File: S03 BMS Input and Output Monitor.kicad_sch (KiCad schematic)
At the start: 29 parts, among them Q4 DMP3018SFV, Q5 DMP3018SFV, U1 LTC1960

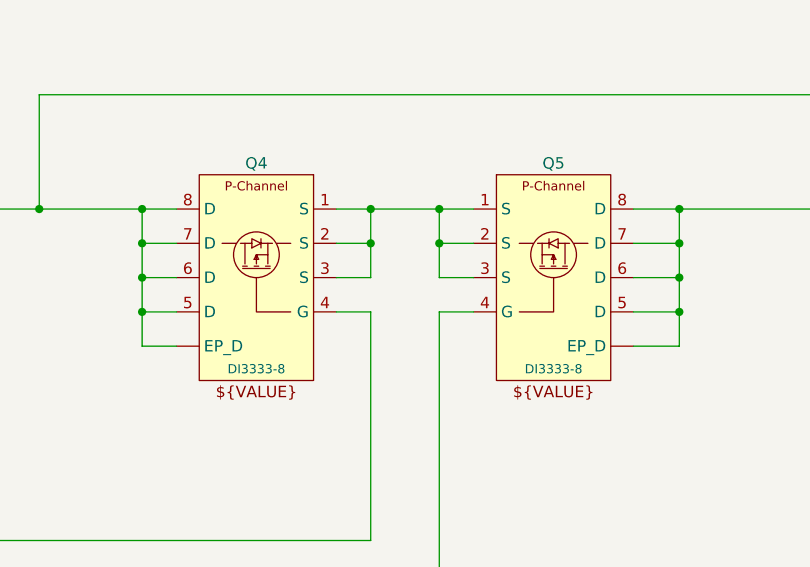
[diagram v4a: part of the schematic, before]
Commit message: Fit DMP3007SCG battery FETs and 1210 snubber resistors
- Q4, Q5, Q12-Q15: DMP3018SFV -> DMP3007SCG-13 (V-DFN3333-8 Type B) on
  KiCad's standard Package_SON:Diodes_PowerDI3333-8, which matches Diodes'
  Type B suggested land apart from 0.1 mm more toe per pad row. The new
  project symbol keeps the old pin positions and numbers D pins 5-8 and
  EP_D all 5, the footprint's single drain pad; all were already one net.
  The unused DMP3018SFV symbol is removed from the project library.
- R41, R45 (SW1/SW2 snubbers): 2.2R 1206 1/4 W -> 2.2R 1% 1210 1/2 W, any
  standard thick film. R41 runs at 75% (0.38 W worst case), R45 at 33%.
- README design-change rows for both.

The PCB still needs Update PCB from Schematic for these and the DAQ UVLO
parts.

Co-Authored-By: Claude Opus 5.5 <noreply@anthropic.com>
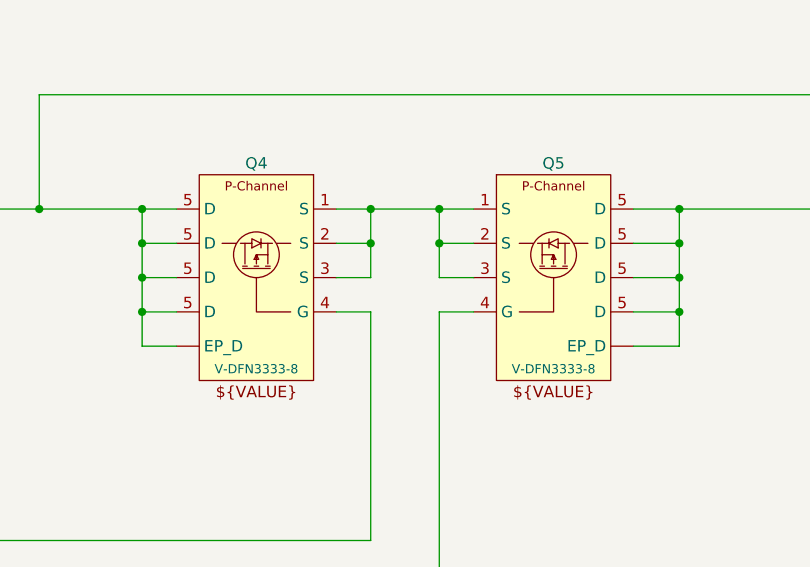
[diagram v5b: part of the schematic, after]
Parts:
- Q4, Q5: value DMP3018SFV -> DMP3007SCG-13; footprint EVO2513-0_5_0-import-fps:Power DI3333-8 B3.3 x 3.3 P0.65 Tab 8-Pin -> Package_SON:Diodes_PowerDI3333-8; symbol Lattech Systems:Transistor P-Channel MOSFET 30V DMP3018SFV Power DI3333-8 -> Lattech Systems:Transistor P-Channel MOSFET 30V DMP3007SCG V-DFN3333-8; ALTIUM_FOOTPRINT DI3333-8 -> V-DFN3333-8; ALTIUM_VALUE DMP3018SFV -> DMP3007SCG-13; MANUFACTURER_PN DMP3018SFV -> DMP3007SCG-13
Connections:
- net DCPATH: no longer Q5.6 (D), Q5.7 (D), Q5.8 (D), Q5.9 (EP_D)
- net DCSENSED: no longer Q4.6 (D), Q4.7 (D), Q4.8 (D), Q4.9 (EP_D)
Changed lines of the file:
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@@
 	)
 	(symbol
-		(lib_id "Lattech Systems:Transistor P-Channel MOSFET  30V DMP3018SFV Power DI3333-8")
+		(lib_id "Lattech Systems:Transistor P-Channel MOSFET 30V DMP3007SCG V-DFN3333-8")
 		(at 260.35 83.82 0)
 		(mirror y)
@@
 			)
 		)
-		(property "Value" "DMP3018SFV"
+		(property "Value" "DMP3007SCG-13"
 			(at 247.65 82.55 0)
 			(hide yes)
@@
 			)
 		)
-		(property "Footprint" "EVO2513-0_5_0-import-fps:Power DI3333-8 B3.3 x 3.3 P0.65 Tab 8-Pin"
+		(property "Footprint" "Package_SON:Diodes_PowerDI3333-8"
 			(at 260.35 83.82 0)
 			(hide yes)
@@
 			)
 		)
-		(property "Description" "Transistor P-Channel MOSFET  30V DMP3018SFV Power DI3333-8"
+		(property "Description" "Transistor P-Channel MOSFET 30V DMP3007SCG-13 V-DFN3333-8 (Type B)"
 			(at 260.35 83.82 0)
 			(hide yes)
@@
 			)
 		)
-		(property "ALTIUM_FOOTPRINT" "DI3333-8"
+		(property "ALTIUM_FOOTPRINT" "V-DFN3333-8"
 			(at 251.46 101.5998 0)
 			(show_name no)
@@
 			)
 		)
-		(property "ALTIUM_VALUE" "DMP3018SFV"
+		(property "ALTIUM_VALUE" "DMP3007SCG-13"
 			(at 270.002 81.026 0)
 			(hide yes)
@@
 			)
 		)
-		(property "MANUFACTURER_PN" "DMP3018SFV"
+		(property "MANUFACTURER_PN" "DMP3007SCG-13"
 			(at 259.842 77.47 0)
 			(hide yes)
@@
 		(pin "5"
 		)
-		(pin "7"
-		)
 		(pin "4"
 		)
 		(pin "2"
-		)
-		(pin "6"
-		)
-		(pin "8"
-		)
-		(pin "9"
 		)
 		(instances
@@
 	)
 	(symbol
-		(lib_id "Lattech Systems:Transistor P-Channel MOSFET  30V DMP3018SFV Power DI3333-8")
+		(lib_id "Lattech Systems:Transistor P-Channel MOSFET 30V DMP3007SCG V-DFN3333-8")
 		(at 275.59 83.82 0)
 		(unit 1)
@@
 			)
 		)
-		(property "Value" "DMP3018SFV"
+		(property "Value" "DMP3007SCG-13"
 			(at 288.29 82.55 0)
 			(hide yes)
@@
 			)
 		)
-		(property "Footprint" "EVO2513-0_5_0-import-fps:Power DI3333-8 B3.3 x 3.3 P0.65 Tab 8-Pin"
+		(property "Footprint" "Package_SON:Diodes_PowerDI3333-8"
 			(at 275.59 83.82 0)
 			(hide yes)
@@
 			)
 		)
-		(property "Description" "Transistor P-Channel MOSFET  30V DMP3018SFV Power DI3333-8"
+		(property "Description" "Transistor P-Channel MOSFET 30V DMP3007SCG-13 V-DFN3333-8 (Type B)"
 			(at 275.59 83.82 0)
 			(hide yes)
@@
 			)
 		)
-		(property "ALTIUM_FOOTPRINT" "DI3333-8"
+		(property "ALTIUM_FOOTPRINT" "V-DFN3333-8"
 			(at 284.48 101.5998 0)
 			(show_name no)
@@
 			)
 		)
-		(property "ALTIUM_VALUE" "DMP3018SFV"
+		(property "ALTIUM_VALUE" "DMP3007SCG-13"
 			(at 265.938 81.026 0)
 			(hide yes)
@@
 			)
 		)
-		(property "MANUFACTURER_PN" "DMP3018SFV"
+		(property "MANUFACTURER_PN" "DMP3007SCG-13"
 			(at 275.082 77.47 0)
 			(hide yes)
@@
 			)
 		)
-		(pin "6"
-		)
 		(pin "3"
 		)
@@
 		(pin "5"
 		)
-		(pin "7"
-		)
 		(pin "4"
 		)
 		(pin "2"
 		)
-		(pin "8"
-		)
-		(pin "9"
-		)
 		(instances

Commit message: R16 to 3 mOhm; note the DAQ/EXT current limits; keep Q18
- R16 0.005R -> 0.003R (Bourns CRE2512-FZ-R003E-3): the LTC1960 breaker
  moves from 18-23 A to 30-38 A. Peak 12 V load is about 7.5 A SBC (90 W)
  + 2.5 A J3 + DAQ, and QE29 packs at ~21 A would sit inside the old trip
  window. S03 note updated.
- S07 note: R53/R71 (1K, 6.6 A limit, up to 7.1 A) exceed J6/J5's 6.5 A
  single contact; raise them to 1.2K or more once the DAQ and EXT loads
  are known. Left at 1K for now: DAQ runs a stand-in, EXT is unused.
- README rows for R16, R53/R71 and Q18 (CSD17304Q3 kept: it works and 15
  units are in field test).

Co-Authored-By: Claude Opus 5.5 <noreply@anthropic.com>
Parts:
- R16: value 0.005R -> 0.003R; ALTIUM_VALUE 0.005R -> 0.003R; MANUFACTURER (none) -> Bourns; MANUFACTURER_PN CRE2512-FZ-R005E-3 -> CRE2512-FZ-R003E-3
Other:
- note added: "R16 breaker latches: 90-115 mV for 15 ms (30-38 A with 3 mR) opens every PowerPath switch, including DC, and sets FA. It clears only when all sources are removed and VPLUS falls below UVLO. ED29 test packs trip at 8 A each (measured); QE29 production packs at 10.5 A. Any figure keyed to 10.5 A applies to QE29 only."
- note removed: "R16 breaker latches: 90-115 mV for 15 ms opens every PowerPath switch, including DC, and sets FA. It clears only when all sources are removed and VPLUS falls below UVLO. ED29 test packs trip at 8 A each (measured); QE29 production packs at 10.5 A. Any figure keyed to 10.5 A applies to QE29 only."
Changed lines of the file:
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@@
 		)
 	)
-	(text "R16 breaker latches: 90-115 mV for 15 ms opens every PowerPath\nswitch, including DC, and sets FA. It clears only when all sources\nare removed and VPLUS falls below UVLO.\nED29 test packs trip at 8 A each (measured); QE29 production packs\nat 10.5 A. Any figure keyed to 10.5 A applies to QE29 only."
+	(text "R16 breaker latches: 90-115 mV for 15 ms (30-38 A with 3 mR)\nopens every PowerPath switch, including DC, and sets FA. It\nclears only when all sources are removed and VPLUS falls below UVLO.\nED29 test packs trip at 8 A each (measured); QE29 production packs\nat 10.5 A. Any figure keyed to 10.5 A applies to QE29 only."
 		(exclude_from_sim no)
 		(at 317.5 184.15 0)
@@
 			)
 		)
-		(property "Value" "0.005R"
+		(property "Value" "0.003R"
 			(at 199.39 172.72 90)
 			(show_name no)
@@
 			)
 		)
-		(property "Description" "Resistor 0.005R 1% 3W 2512"
+		(property "Description" "Resistor 0.003R 1% 3W 2512"
 			(at 212.09 172.72 90)
 			(hide yes)
@@
 			)
 		)
-		(property "MANUFACTURER" ""
+		(property "MANUFACTURER" "Bourns"
 			(at 207.772 168.91 90)
 			(hide yes)
@@
 			)
 		)
-		(property "MANUFACTURER_PN" "CRE2512-FZ-R005E-3"
+		(property "MANUFACTURER_PN" "CRE2512-FZ-R003E-3"
 			(at 207.772 168.91 90)
 			(hide yes)
@@
 			)
 		)
-		(property "ALTIUM_VALUE" "0.005R"
+		(property "ALTIUM_VALUE" "0.003R"
 			(at 214.376 176.784 90)
 			(hide yes)

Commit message: U11 PCAL9714HNMP 3D model; FET zone reshaping; R23/R82-R85 DNP
- U11 moves to a project-library copy of HVQFN-24-1EP_4x4mm_P0.5mm_EP2.6x2.6mm
  linked to ${KIPRJMOD}/PCAL9714HNMP.stp (STEP later embedded; file not kept). Schematic and Lattech
  symbol point at the project copy.
- Board updated from the schematic (symbol pin data on the swapped
  footprints) and zone fills reshaped around the FETs.
- R23, R82-R85 (NEQ) set DNP in the schematic and on the board.

DRC: 0 errors, 0 unconnected, 0 schematic parity issues. ERC: 0 violations.

Co-Authored-By: Claude Opus 5.5 <noreply@anthropic.com>
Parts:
- R23, R82: now not fitted
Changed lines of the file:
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@@
 		(on_board yes)
 		(in_pos_files yes)
-		(dnp no)
+		(dnp yes)
 		(property "Reference" "R23"
 			(at 113.03 77.724 0)
@@
 		(on_board yes)
 		(in_pos_files yes)
-		(dnp no)
+		(dnp yes)
 		(property "Reference" "R82"
 			(at 209.55 166.624 0)
